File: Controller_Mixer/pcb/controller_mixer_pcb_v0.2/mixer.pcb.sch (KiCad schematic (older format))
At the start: 75 parts

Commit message: controller_mixer_pcb_v0.2 - Irgendwo ist angeblich ein Kurzschluss sagt der Debugger aber ich find ihn nicht...
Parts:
- added J? (x5): Conn_01x03, Connector_JST:JST_XH_B3B-XH-A_1x03_P2.50mm_Vertical, symbol Connector_Generic:Conn_01x03
- J1, J17, J18, J2, J20, J21, J22, J23, J24, J25, J26, J27, J28, J29, J3, J30, J31, J32, J33, J34, J35, J36, J37, J38, J39, J4, J40, J43, J5, J6, J60, J61, J62, J63, J64, J65, J66, J67, J7, J8: renamed from J?; footprint (none) -> Connector_JST:JST_XH_B3B-XH-A_1x03_P2.50mm_Vertical
- J10, J11, J12, J13, J14, J15, J16, J44, J45, J46, J47, J48, J49, J50, J51, J52, J53, J9: renamed from J?; footprint (none) -> Connector_JST:JST_XH_B2B-XH-A_1x02_P2.50mm_Vertical
- J41, J42: renamed from J?; footprint (none) -> Connector_JST:JST_XH_B4B-XH-A_1x04_P2.50mm_Vertical
- J54, J55, J56, J57, J58, J59: renamed from J?; footprint (none) -> Connector_JST:JST_XH_B5B-XH-A_1x05_P2.50mm_Vertical
- U1, U2, U3, U4, U6, U7, U8: renamed from U?; footprint (none) -> Package_DIP:DIP-16_W7.62mm
- U5: renamed from U?; footprint (none) -> teensy:Teensy41
- gave numbers to parts that had none: 1
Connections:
- net labels added: neopixel, pin14, pin15, pin18, pin28, pin29
- net labels removed: mux_ch5, neostrip
- no-connect marks 20 -> 22
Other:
- moved on the sheet: J1, J10, J11, J12, J13, J14, J15, J16, J17, J18, J19, J2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

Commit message: controller_mixer_pcb_v0.2 - edits
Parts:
- gave numbers to parts that had none: 5

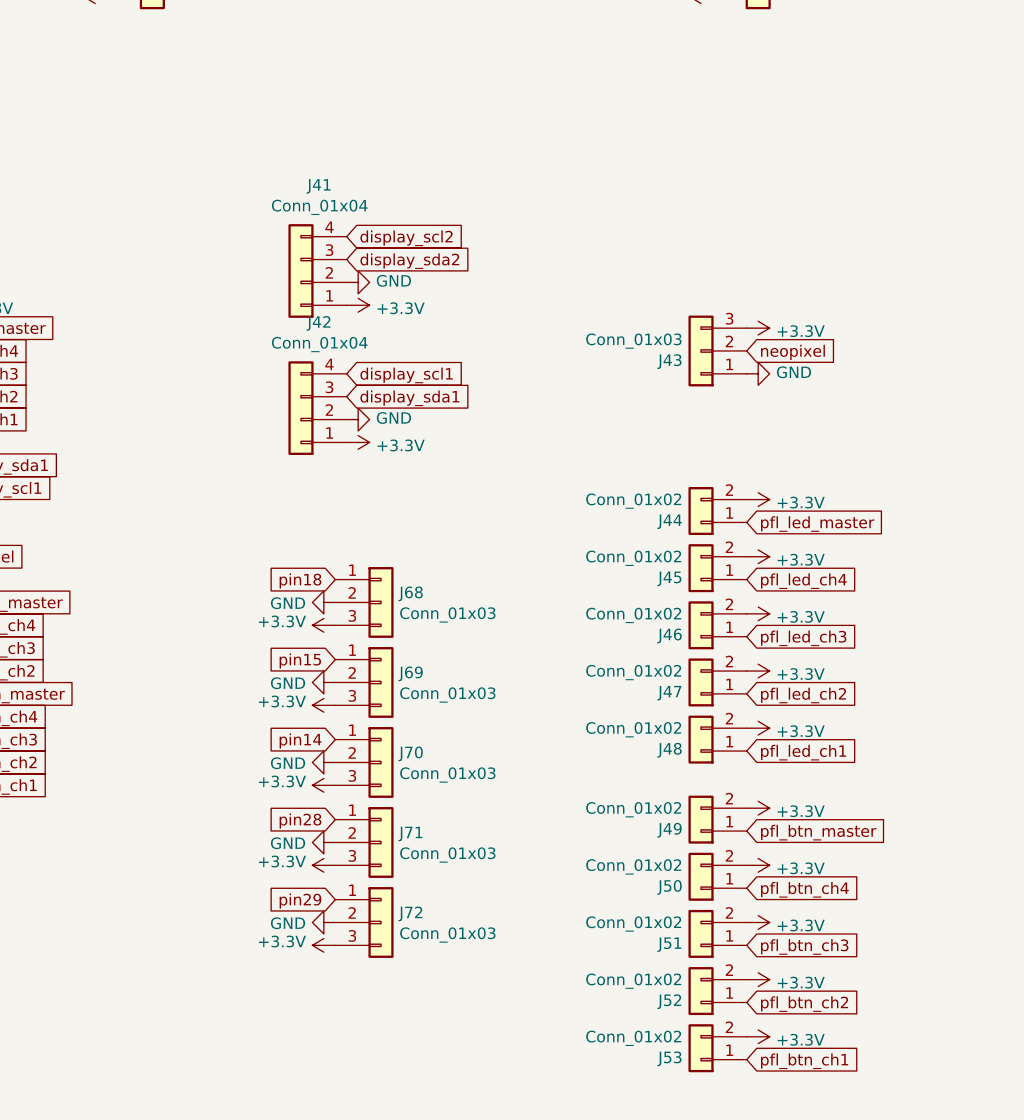
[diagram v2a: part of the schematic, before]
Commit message: add LED Matrix vu
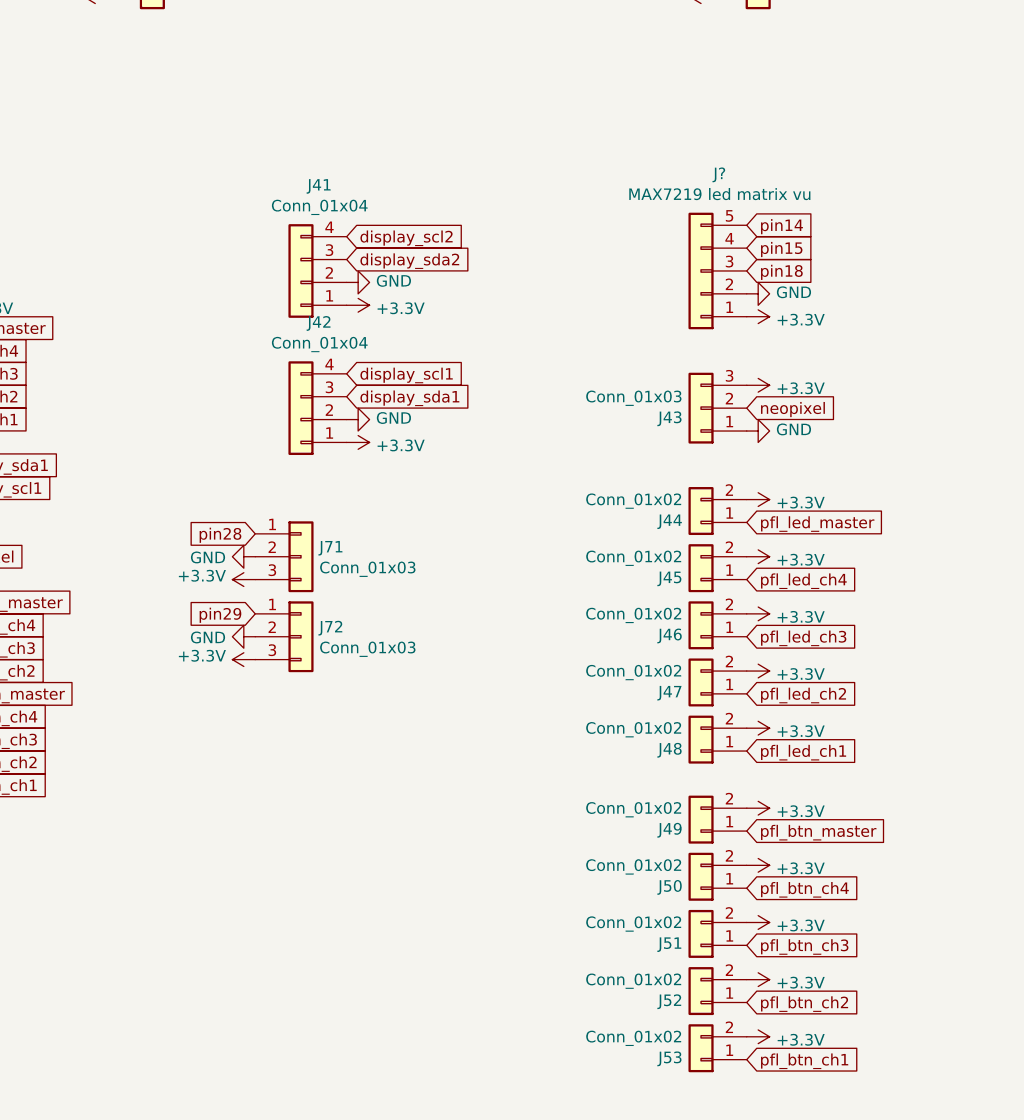
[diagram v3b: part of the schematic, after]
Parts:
- removed J68, J69, J70: Conn_01x03, Connector_JST:JST_XH_B3B-XH-A_1x03_P2.50mm_Vertical, symbol Connector_Generic:Conn_01x03
- added J?: MAX7219 led matrix vu, symbol mixer.pcb:Connector_Generic_Conn_01x05
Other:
- moved on the sheet: J43, J71, J72
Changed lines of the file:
@@
 	-1   0    0    -1
 $EndComp
-Text GLabel 11250 5500 2    50   Input ~ 0
+Text GLabel 11250 5750 2    50   Input ~ 0
 neopixel
 $Comp
 L power:GND #PWR0207
 U 1 1 607656B6
-P 11250 5600
-F 0 "#PWR0207" H 11250 5350 50  0001 C CNN
-F 1 "GND" V 11255 5472 50  0000 R CNN
-F 2 "" H 11250 5600 50  0001 C CNN
-F 3 "" H 11250 5600 50  0001 C CNN
-	1    11250 5600
+P 11250 5850
+F 0 "#PWR0207" H 11250 5600 50  0001 C CNN
+F 1 "GND" V 11255 5722 50  0000 R CNN
+F 2 "" H 11250 5850 50  0001 C CNN
+F 3 "" H 11250 5850 50  0001 C CNN
+	1    11250 5850
 	0    -1   -1   0
 $EndComp
@@
 L power:+3.3V #PWR0206
 U 1 1 60764E8F
-P 11250 5400
-F 0 "#PWR0206" H 11250 5250 50  0001 C CNN
-F 1 "+3.3V" V 11265 5528 50  0000 L CNN
-F 2 "" H 11250 5400 50  0001 C CNN
-F 3 "" H 11250 5400 50  0001 C CNN
-	1    11250 5400
+P 11250 5650
+F 0 "#PWR0206" H 11250 5500 50  0001 C CNN
+F 1 "+3.3V" V 11265 5778 50  0000 L CNN
+F 2 "" H 11250 5650 50  0001 C CNN
+F 3 "" H 11250 5650 50  0001 C CNN
+	1    11250 5650
 	0    1    1    0
 $EndComp
@@
 L Connector_Generic:Conn_01x03 J43
 U 1 1 607646F2
-P 11050 5500
-F 0 "J43" H 11130 5542 50  0000 L CNN
-F 1 "Conn_01x03" H 11130 5451 50  0000 L CNN
-F 2 "Connector_JST:JST_XH_B3B-XH-A_1x03_P2.50mm_Vertical" H 11050 5500 50  0001 C CNN
-F 3 "~" H 11050 5500 50  0001 C CNN
-	1    11050 5500
+P 11050 5750
+F 0 "J43" H 11130 5792 50  0000 L CNN
+F 1 "Conn_01x03" H 11130 5701 50  0000 L CNN
+F 2 "Connector_JST:JST_XH_B3B-XH-A_1x03_P2.50mm_Vertical" H 11050 5750 50  0001 C CNN
+F 3 "~" H 11050 5750 50  0001 C CNN
+	1    11050 5750
 	-1   0    0    1
 $EndComp
@@
 L power:+3.3V #PWR0247
 U 1 1 6087B9AE
-P 9450 8100
-F 0 "#PWR0247" H 9450 7950 50  0001 C CNN
-F 1 "+3.3V" V 9465 8228 50  0000 L CNN
-F 2 "" H 9450 8100 50  0001 C CNN
-F 3 "" H 9450 8100 50  0001 C CNN
-	1    9450 8100
+P 9100 6850
+F 0 "#PWR0247" H 9100 6700 50  0001 C CNN
+F 1 "+3.3V" V 9115 6978 50  0000 L CNN
+F 2 "" H 9100 6850 50  0001 C CNN
+F 3 "" H 9100 6850 50  0001 C CNN
+	1    9100 6850
 	0    -1   -1   0
 $EndComp
@@
 L power:GND #PWR0246
 U 1 1 6087B9A8
-P 9450 8000
-F 0 "#PWR0246" H 9450 7750 50  0001 C CNN
-F 1 "GND" V 9455 7872 50  0000 R CNN
-F 2 "" H 9450 8000 50  0001 C CNN
-F 3 "" H 9450 8000 50  0001 C CNN
-	1    9450 8000
+P 9100 6750
+F 0 "#PWR0246" H 9100 6500 50  0001 C CNN
+F 1 "GND" V 9105 6622 50  0000 R CNN
+F 2 "" H 9100 6750 50  0001 C CNN
+F 3 "" H 9100 6750 50  0001 C CNN
+	1    9100 6750
 	0    1    1    0
 $EndComp
@@
 L Connector_Generic:Conn_01x03 J72
 U 1 1 6087B9A2
-P 9650 8000
-F 0 "J72" H 9730 8042 50  0000 L CNN
-F 1 "Conn_01x03" H 9730 7951 50  0000 L CNN
-F 2 "Connector_JST:JST_XH_B3B-XH-A_1x03_P2.50mm_Vertical" H 9650 8000 50  0001 C CNN
-F 3 "~" H 9650 8000 50  0001 C CNN
-	1    9650 8000
+P 9300 6750
+F 0 "J72" H 9380 6792 50  0000 L CNN
+F 1 "Conn_01x03" H 9380 6701 50  0000 L CNN
+F 2 "Connector_JST:JST_XH_B3B-XH-A_1x03_P2.50mm_Vertical" H 9300 6750 50  0001 C CNN
+F 3 "~" H 9300 6750 50  0001 C CNN
+	1    9300 6750
 	1    0    0    -1
 $EndComp
@@
 L power:+3.3V #PWR0245
 U 1 1 6086F86A
-P 9450 7750
-F 0 "#PWR0245" H 9450 7600 50  0001 C CNN
-F 1 "+3.3V" V 9465 7878 50  0000 L CNN
-F 2 "" H 9450 7750 50  0001 C CNN
-F 3 "" H 9450 7750 50  0001 C CNN
-	1    9450 7750
+P 9100 6500
+F 0 "#PWR0245" H 9100 6350 50  0001 C CNN
+F 1 "+3.3V" V 9115 6628 50  0000 L CNN
+F 2 "" H 9100 6500 50  0001 C CNN
+F 3 "" H 9100 6500 50  0001 C CNN
+	1    9100 6500
 	0    -1   -1   0
 $EndComp
@@
 L power:GND #PWR0244
 U 1 1 6086F864
-P 9450 7650
-F 0 "#PWR0244" H 9450 7400 50  0001 C CNN
-F 1 "GND" V 9455 7522 50  0000 R CNN
-F 2 "" H 9450 7650 50  0001 C CNN
-F 3 "" H 9450 7650 50  0001 C CNN
-	1    9450 7650
+P 9100 6400
+F 0 "#PWR0244" H 9100 6150 50  0001 C CNN
+F 1 "GND" V 9105 6272 50  0000 R CNN
+F 2 "" H 9100 6400 50  0001 C CNN
+F 3 "" H 9100 6400 50  0001 C CNN
+	1    9100 6400
 	0    1    1    0
 $EndComp
@@
 L Connector_Generic:Conn_01x03 J71
 U 1 1 6086F85E
-P 9650 7650
-F 0 "J71" H 9730 7692 50  0000 L CNN
-F 1 "Conn_01x03" H 9730 7601 50  0000 L CNN
-F 2 "Connector_JST:JST_XH_B3B-XH-A_1x03_P2.50mm_Vertical" H 9650 7650 50  0001 C CNN
-F 3 "~" H 9650 7650 50  0001 C CNN
-	1    9650 7650
+P 9300 6400
+F 0 "J71" H 9380 6442 50  0000 L CNN
+F 1 "Conn_01x03" H 9380 6351 50  0000 L CNN
+F 2 "Connector_JST:JST_XH_B3B-XH-A_1x03_P2.50mm_Vertical" H 9300 6400 50  0001 C CNN
+F 3 "~" H 9300 6400 50  0001 C CNN
+	1    9300 6400
 	1    0    0    -1
 $EndComp
-$Comp
-L power:+3.3V #PWR0243
-U 1 1 60863798
-P 9450 7400
-F 0 "#PWR0243" H 9450 7250 50  0001 C CNN
-F 1 "+3.3V" V 9465 7528 50  0000 L CNN
-F 2 "" H 9450 7400 50  0001 C CNN
-F 3 "" H 9450 7400 50  0001 C CNN
-	1    9450 7400
-	0    -1   -1   0
-$EndComp
-$Comp
-L power:GND #PWR0242
-U 1 1 60863792
-P 9450 7300
-F 0 "#PWR0242" H 9450 7050 50  0001 C CNN
-F 1 "GND" V 9455 7172 50  0000 R CNN
-F 2 "" H 9450 7300 50  0001 C CNN
-F 3 "" H 9450 7300 50  0001 C CNN
-	1    9450 7300
-	0    1    1    0
-$EndComp
-$Comp
-L Connector_Generic:Conn_01x03 J70
-U 1 1 6086378C
-P 9650 7300
-F 0 "J70" H 9730 7342 50  0000 L CNN
-F 1 "Conn_01x03" H 9730 7251 50  0000 L CNN
-F 2 "Connector_JST:JST_XH_B3B-XH-A_1x03_P2.50mm_Vertical" H 9650 7300 50  0001 C CNN
-F 3 "~" H 9650 7300 50  0001 C CNN
-	1    9650 7300
-	1    0    0    -1
-$EndComp
-$Comp
-L power:+3.3V #PWR0241
-U 1 1 6085773D
-P 9450 7050
-F 0 "#PWR0241" H 9450 6900 50  0001 C CNN
-F 1 "+3.3V" V 9465 7178 50  0000 L CNN
-F 2 "" H 9450 7050 50  0001 C CNN
-F 3 "" H 9450 7050 50  0001 C CNN
-	1    9450 7050
-	0    -1   -1   0
-$EndComp
-$Comp
-L power:GND #PWR0240
-U 1 1 60857737
-P 9450 6950
-F 0 "#PWR0240" H 9450 6700 50  0001 C CNN
-F 1 "GND" V 9455 6822 50  0000 R CNN
-F 2 "" H 9450 6950 50  0001 C CNN
-F 3 "" H 9450 6950 50  0001 C CNN
-	1    9450 6950
-	0    1    1    0
-$EndComp
-$Comp
-L Connector_Generic:Conn_01x03 J69
-U 1 1 60857731
-P 9650 6950
-F 0 "J69" H 9730 6992 50  0000 L CNN
-F 1 "Conn_01x03" H 9730 6901 50  0000 L CNN
-F 2 "Connector_JST:JST_XH_B3B-XH-A_1x03_P2.50mm_Vertical" H 9650 6950 50  0001 C CNN
-F 3 "~" H 9650 6950 50  0001 C CNN
-	1    9650 6950
-	1    0    0    -1
-$EndComp
-$Comp
-L power:+3.3V #PWR0239
-U 1 1 607EDEDA
-P 9450 6700
-F 0 "#PWR0239" H 9450 6550 50  0001 C CNN
-F 1 "+3.3V" V 9465 6828 50  0000 L CNN
-F 2 "" H 9450 6700 50  0001 C CNN
-F 3 "" H 9450 6700 50  0001 C CNN
-	1    9450 6700
-	0    -1   -1   0
-$EndComp
-$Comp
-L power:GND #PWR0238
-U 1 1 607EDED4
-P 9450 6600
-F 0 "#PWR0238" H 9450 6350 50  0001 C CNN
-F 1 "GND" V 9455 6472 50  0000 R CNN
-F 2 "" H 9450 6600 50  0001 C CNN
-F 3 "" H 9450 6600 50  0001 C CNN
-	1    9450 6600
-	0    1    1    0
-$EndComp
-$Comp
-L Connector_Generic:Conn_01x03 J68
-U 1 1 607EDECE
-P 9650 6600
-F 0 "J68" H 9730 6642 50  0000 L CNN
-F 1 "Conn_01x03" H 9730 6551 50  0000 L CNN
-F 2 "Connector_JST:JST_XH_B3B-XH-A_1x03_P2.50mm_Vertical" H 9650 6600 50  0001 C CNN
-F 3 "~" H 9650 6600 50  0001 C CNN
-	1    9650 6600
-	1    0    0    -1
-$EndComp
-Text GLabel 9450 7900 0    50   Input ~ 0
+Text GLabel 9100 6650 0    50   Input ~ 0
 pin29
-Text GLabel 9450 7550 0    50   Input ~ 0
+Text GLabel 9100 6300 0    50   Input ~ 0
 pin28
-Text GLabel 9450 7200 0    50   Input ~ 0
+Text GLabel 11250 4950 2    50   Input ~ 0
 pin14
-Text GLabel 9450 6850 0    50   Input ~ 0
+Text GLabel 11250 5050 2    50   Input ~ 0
 pin15
-Text GLabel 9450 6500 0    50   Input ~ 0
+Text GLabel 11250 5150 2    50   Input ~ 0
 pin18
 $Comp
@@
 	0    -1   -1   0
 $EndComp
+$Comp
+L mixer.pcb:Connector_Generic_Conn_01x05 J?
+U 1 1 5FFCCC67
+P 11050 5150
+F 0 "J?" H 10968 4725 50  0000 C CNN
+F 1 "MAX7219 led matrix vu" H 10968 4816 50  0000 C CNN
+F 2 "" H 11050 5150 50  0001 C CNN
+F 3 "" H 11050 5150 50  0001 C CNN
+	1    11050 5150
+	-1   0    0    1
+$EndComp
+$Comp
+L mixer.pcb:+3.3V #PWR?
+U 1 1 5FFD070A
+P 11250 5350
+F 0 "#PWR?" H 11250 5200 50  0001 C CNN
+F 1 "+3.3V" V 11265 5478 50  0000 L CNN
+F 2 "" H 11250 5350 50  0001 C CNN
+F 3 "" H 11250 5350 50  0001 C CNN
+	1    11250 5350
+	0    1    1    0
+$EndComp
+$Comp
+L power:GND #PWR?
+U 1 1 5FFD1DCA
+P 11250 5250
+F 0 "#PWR?" H 11250 5000 50  0001 C CNN
+F 1 "GND" V 11255 5122 50  0000 R CNN
+F 2 "" H 11250 5250 50  0001 C CNN
+F 3 "" H 11250 5250 50  0001 C CNN
+	1    11250 5250
+	0    -1   -1   0
+$EndComp

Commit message: fix versuch
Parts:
- U5: symbol teensy:Teensy4.1 -> mixer.pcb-rescue:Teensy4.1-teensy

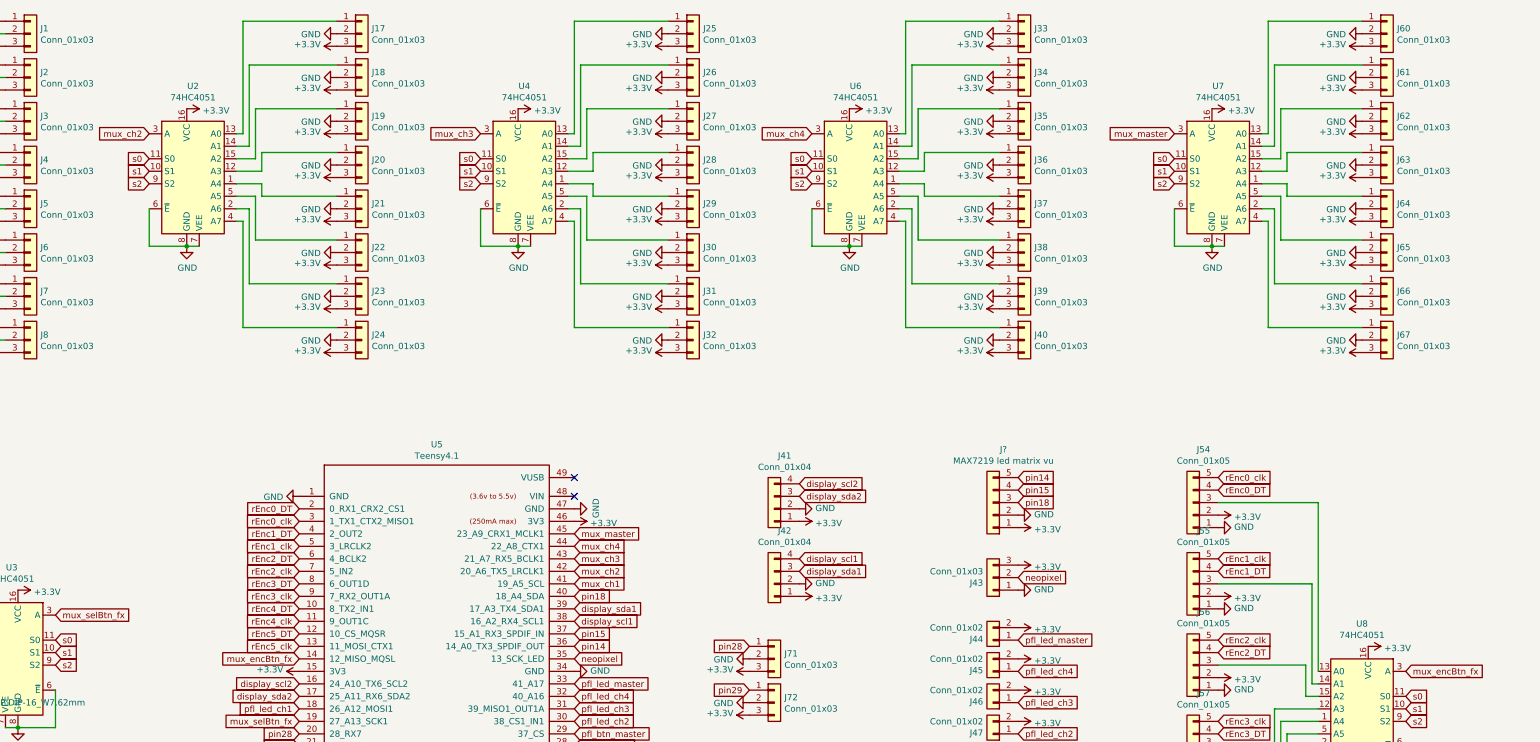
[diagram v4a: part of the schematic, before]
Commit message: corrections mixer_pcb
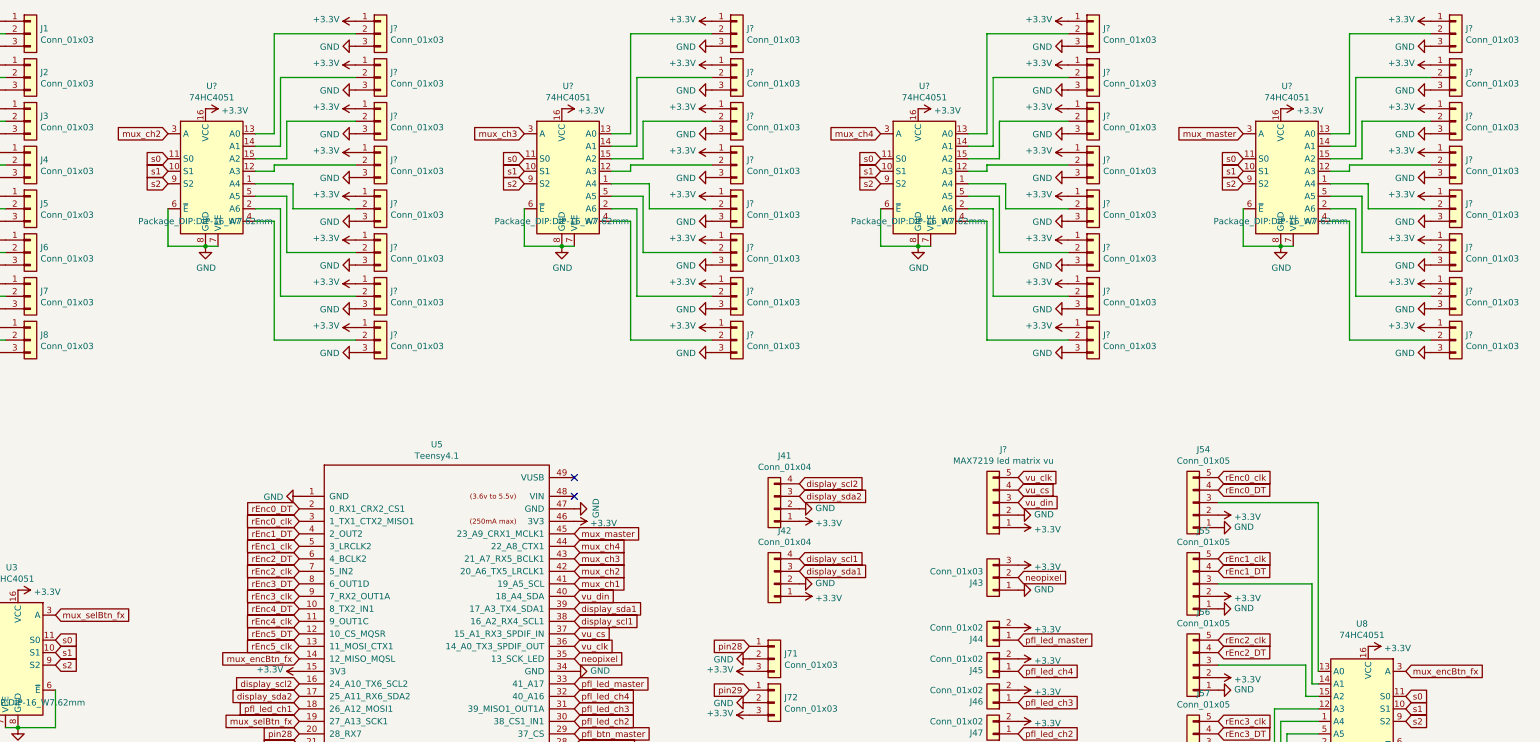
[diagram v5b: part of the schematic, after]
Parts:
- removed J17, J18, J20, J21, J22, J23, J24, J25, J26, J27, J28, J29, J30, J31, J32, J33, J34, J35, J36, J37, J38, J39, J40, J60, J61, J62, J63, J64, J65, J66, J67: Conn_01x03, Connector_JST:JST_XH_B3B-XH-A_1x03_P2.50mm_Vertical, symbol Connector_Generic:Conn_01x03
- removed J19: Conn_01x03, symbol Connector_Generic:Conn_01x03
- removed U2, U4, U6, U7: 74HC4051, Package_DIP:DIP-16_W7.62mm, symbol 74xx:74HC4051
- added J? (x32): Conn_01x03, Connector_JST:JST_XH_B3B-XH-A_1x03_P2.50mm_Vertical, symbol Connector_Generic:Conn_01x03
- added U? (x4): 74HC4051, Package_DIP:DIP-16_W7.62mm, symbol 74xx:74HC4051
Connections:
- net +3V3: now also J?.1 (Pin_1), J?.1 (Pin_1), J?.1 (Pin_1), J?.1 (Pin_1), J?.1 (Pin_1), J?.1 (Pin_1), J?.1 (Pin_1), J?.1 (Pin_1), J?.1 (Pin_1), J?.1 (Pin_1), J?.1 (Pin_1), J?.1 (Pin_1), J?.1 (Pin_1), J?.1 (Pin_1), J?.1 (Pin_1), J?.1 (Pin_1), J?.1 (Pin_1), J?.1 (Pin_1), J?.1 (Pin_1), J?.1 (Pin_1), J?.1 (Pin_1), J?.1 (Pin_1), J?.1 (Pin_1), J?.1 (Pin_1), J?.1 (Pin_1), J?.1 (Pin_1), J?.1 (Pin_1), J?.1 (Pin_1), J?.1 (Pin_1), J?.1 (Pin_1), J?.1 (Pin_1), J?.1 (Pin_1), U?.16 (VCC), U?.16 (VCC), U?.16 (VCC), U?.16 (VCC)
- net GND: now also J?.3 (Pin_3), J?.3 (Pin_3), J?.3 (Pin_3), J?.3 (Pin_3), J?.3 (Pin_3), J?.3 (Pin_3), J?.3 (Pin_3), J?.3 (Pin_3), J?.3 (Pin_3), J?.3 (Pin_3), J?.3 (Pin_3), J?.3 (Pin_3), J?.3 (Pin_3), J?.3 (Pin_3), J?.3 (Pin_3), J?.3 (Pin_3), J?.3 (Pin_3), J?.3 (Pin_3), J?.3 (Pin_3), J?.3 (Pin_3), J?.3 (Pin_3), J?.3 (Pin_3), J?.3 (Pin_3), J?.3 (Pin_3), J?.3 (Pin_3), J?.3 (Pin_3), J?.3 (Pin_3), J?.3 (Pin_3), J?.3 (Pin_3), J?.3 (Pin_3), J?.3 (Pin_3), J?.3 (Pin_3), U?.6 (~E), U?.6 (~E), U?.6 (~E), U?.6 (~E), U?.7 (VEE), U?.7 (VEE), U?.7 (VEE), U?.7 (VEE), U?.8 (GND), U?.8 (GND), U?.8 (GND), U?.8 (GND)
- net mux_ch2: now also U?.3 (A)
- net mux_ch3: now also U?.3 (A)
- net mux_ch4: now also U?.3 (A)
- net mux_master: now also U?.3 (A)
- net s0: now also U?.11 (S0), U?.11 (S0), U?.11 (S0), U?.11 (S0)
- net s1: now also U?.10 (S1), U?.10 (S1), U?.10 (S1), U?.10 (S1)
- net s2: now also U?.9 (S2), U?.9 (S2), U?.9 (S2), U?.9 (S2)
- net pin14 renamed vu_clk
- net pin15 renamed vu_cs
- net pin18 renamed vu_din
- new net: J?.2 (Pin_2), U?.2 (A6) (x4)
- new net: J?.2 (Pin_2), U?.12 (A3) (x4)
- new net: J?.2 (Pin_2), U?.15 (A2) (x4)
- new net: J?.2 (Pin_2), U?.14 (A1) (x4)
- new net: J?.2 (Pin_2), U?.4 (A7) (x4)
- new net: J?.2 (Pin_2), U?.5 (A5) (x4)
- new net: J?.2 (Pin_2), U?.1 (A4) (x4)
- new net: J?.2 (Pin_2), U?.13 (A0) (x4)
